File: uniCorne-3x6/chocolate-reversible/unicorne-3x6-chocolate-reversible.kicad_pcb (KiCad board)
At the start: 2 copper layers, 133.8 x 91.4 mm, 98 parts, among them J1 MJ-4PP-9, J2 Conn_01x05, J3 Conn_01x02, J4 Conn_01x03, SW1 SW_CHOC_HS, SW10 SW_CHOC_HS, SW11 SW_CHOC_HS, SW12 SW_CHOC_HS, SW13 SW_CHOC_HS, SW14 SW_CHOC_HS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

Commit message: small tweak
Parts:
- U1: footprint TB2086_MISC:ProMicro-ish-dn-rev-unrouted_3x5 -> TB2086_MISC:ProMicro-ish-dn-rev-unrouted_3x6
- moved R3 1.14 mm to (184.1, 109.9)
- moved R4 1.14 mm to (184.1, 111.8)
- moved JP9 0.70 mm to (188.2, 110.8)
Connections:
- PSW1 pad 1: unconnected-(PSW1-A-Pad1) -> BAT+
- PSW1 pad 3: BAT+ -> unconnected-(PSW1-C-Pad3)
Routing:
- net unconnected-(U1-RAW-Pad24): track 29.2 -> 11.0 mm
- net LED: track 62.4 -> 79.2 mm, vias 4 -> 5
- net DATA: track 64.2 -> 77.0 mm
- net unconnected-(PSW1-A-Pad1): track 6.23 -> 0.00 mm
- net col0: track 231.5 -> 226.1 mm
- net unconnected-(PSW1-C-Pad3): track 0.00 -> 5.32 mm
- net SDA: track 72.7 -> 68.2 mm
- net RESET: track 58.9 -> 62.9 mm
- net row3: track 109.5 -> 105.8 mm
- net BAT+: track 17.4 -> 14.0 mm
- net Net-(JP9-C): track 16.3 -> 14.0 mm
- net row0: track 166.0 -> 168.1 mm, vias 1 -> 2
- net col4: track 181.1 -> 179.3 mm
- net VCC: track 586.6 -> 584.9 mm, vias 3 -> 4
- net col5: track 141.9 -> 140.6 mm
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
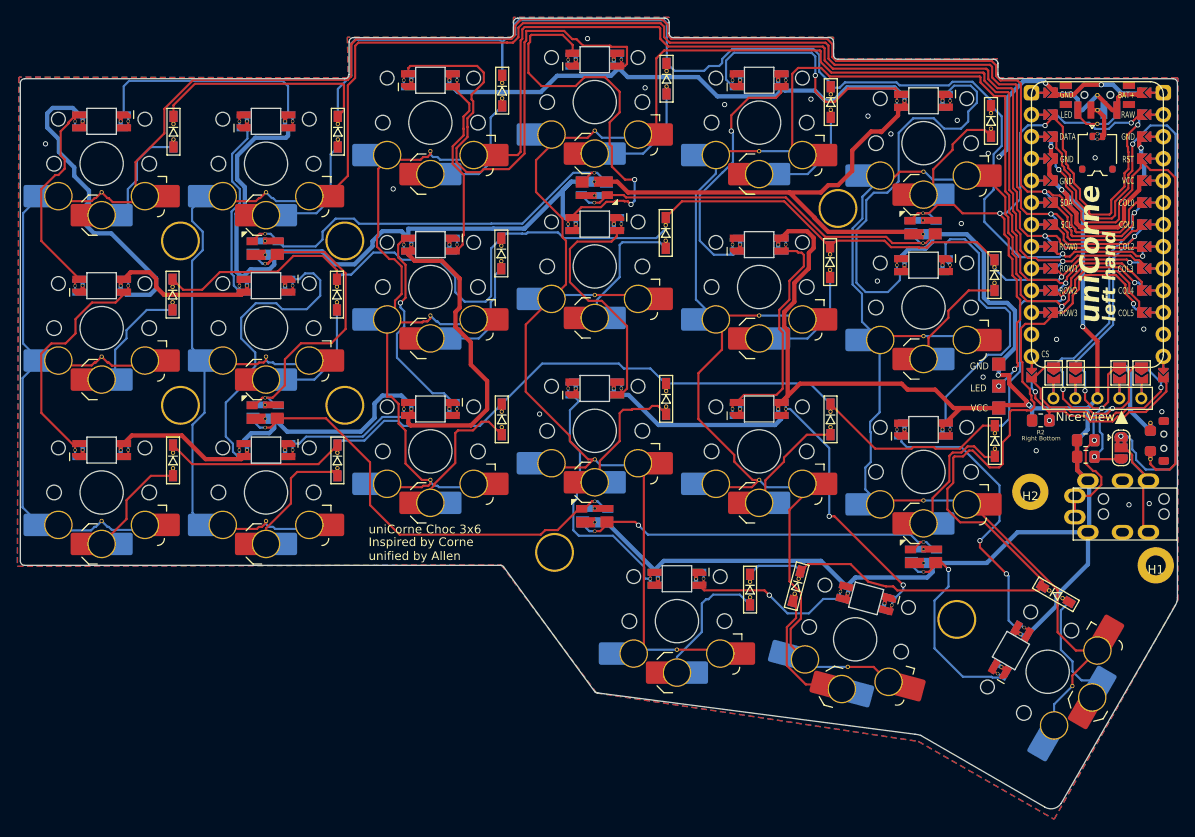
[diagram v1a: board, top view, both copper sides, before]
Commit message: amended footprint for LED
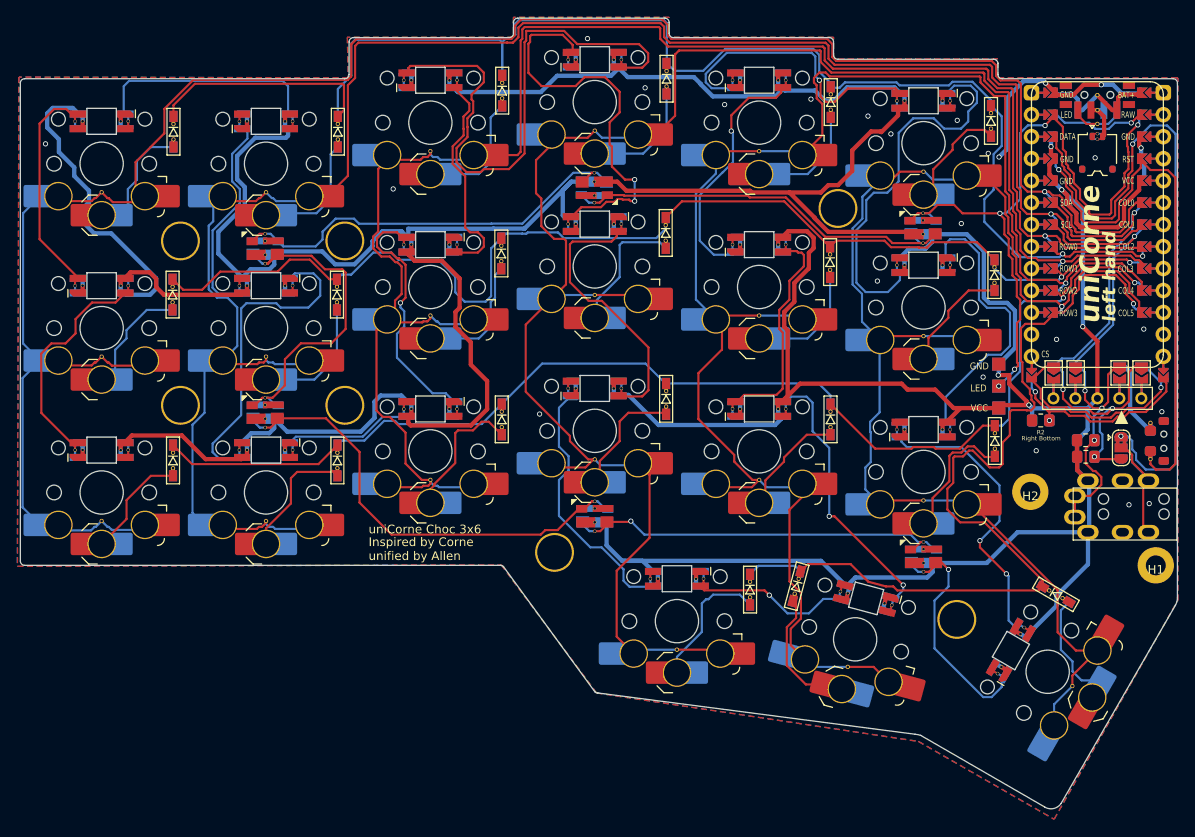
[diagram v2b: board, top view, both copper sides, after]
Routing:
- net VCC: track 584.9 -> 590.1 mm
- net Net-(L15-DIN): track 23.6 -> 28.8 mm
- net Net-(L3-DIN): track 60.8 -> 65.0 mm
- net Net-(L5-DIN): track 29.7 -> 33.6 mm
- net Net-(L3-DOUT): track 21.5 -> 25.4 mm
- net Net-(L10-DIN): track 27.5 -> 31.3 mm
- net Net-(L2-DIN): track 21.1 -> 24.4 mm
- net Net-(L17-DOUT): track 28.5 -> 31.3 mm
- net col4: track 179.3 -> 177.0 mm
- net Net-(L1-DOUT): track 22.8 -> 25.1 mm
- net col2: track 190.4 -> 192.4 mm
- net col1: track 207.3 -> 209.2 mm
- net col3: track 195.2 -> 197.0 mm
- net Net-(L21-DIN): track 25.2 -> 26.9 mm
- net Net-(L14-DOUT): track 35.6 -> 37.2 mm
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
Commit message: small tweak
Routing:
- net Net-(L12-DIN): track 33.0 -> 31.4 mm
- net col1: track 209.2 -> 210.0 mm

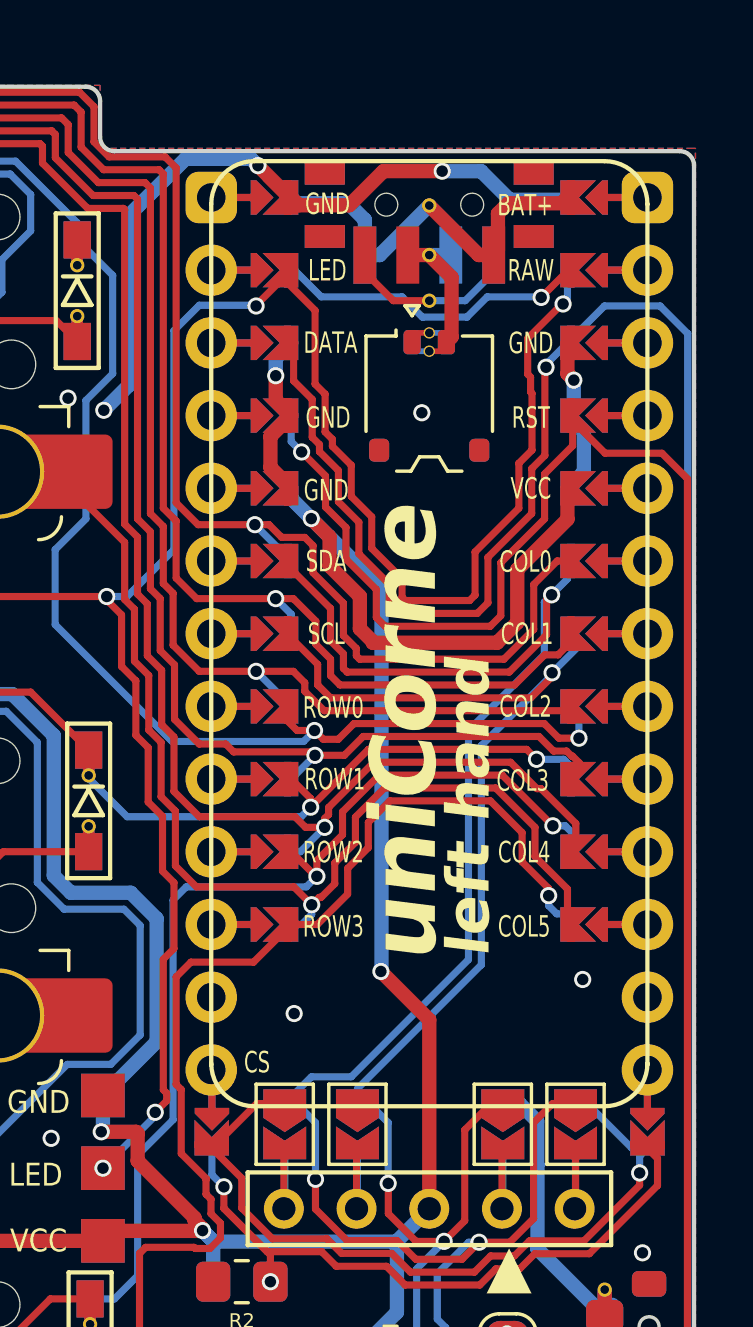
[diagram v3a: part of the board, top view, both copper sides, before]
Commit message: fixed footprint for promicro-ish 3x6
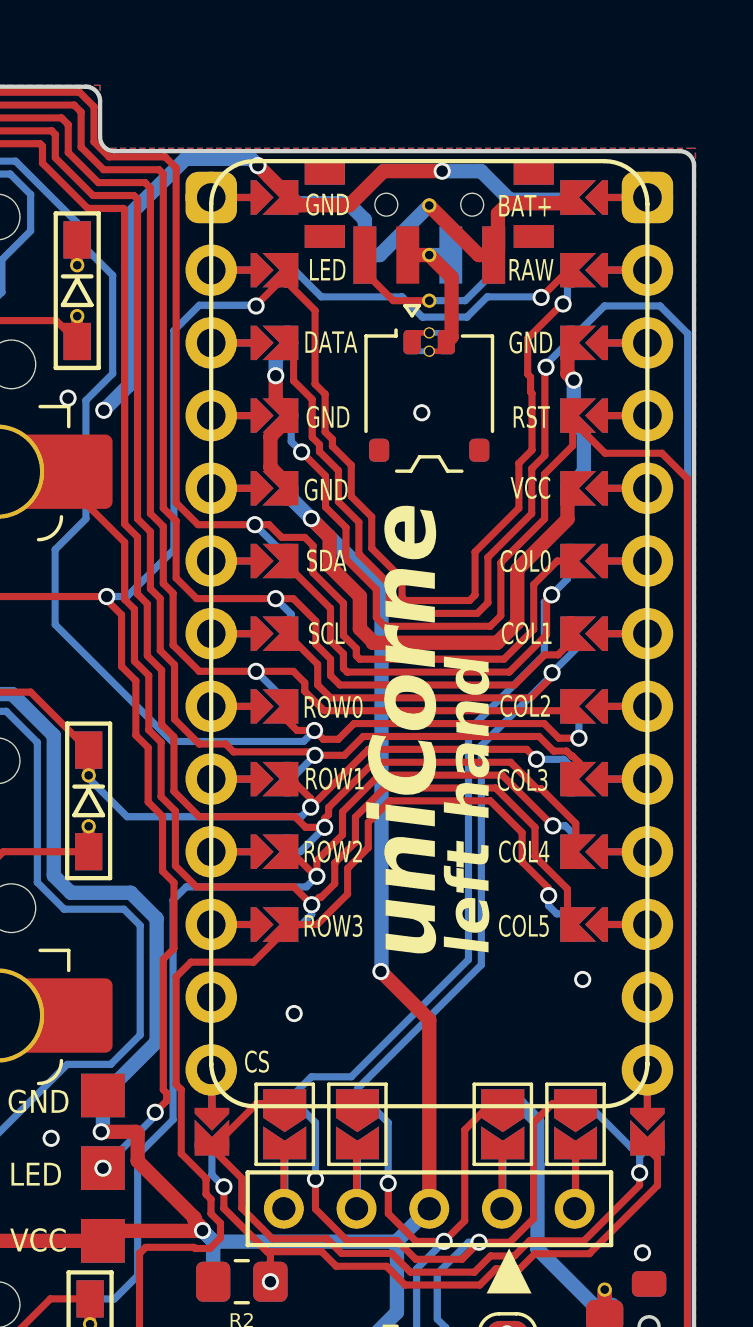
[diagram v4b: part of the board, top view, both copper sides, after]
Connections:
- U1 pad 12: IS_LEFT -> CS
- U1 pad 13: CS -> IS_LEFT
